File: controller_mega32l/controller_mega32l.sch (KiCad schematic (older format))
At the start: 82 parts, among them IC1 ATMEGA32-A, IC2 MAX481CPA, J1 RJ45, K1 CONN_PWR_OUT, P1 CONN_PWR_IN, P2 CONN_PWM_OUT, P3 CONN_3X2, P4 CONN_JTAG, P5 CONN_ADC, P6 CONN_GPIO, Q1 NPN

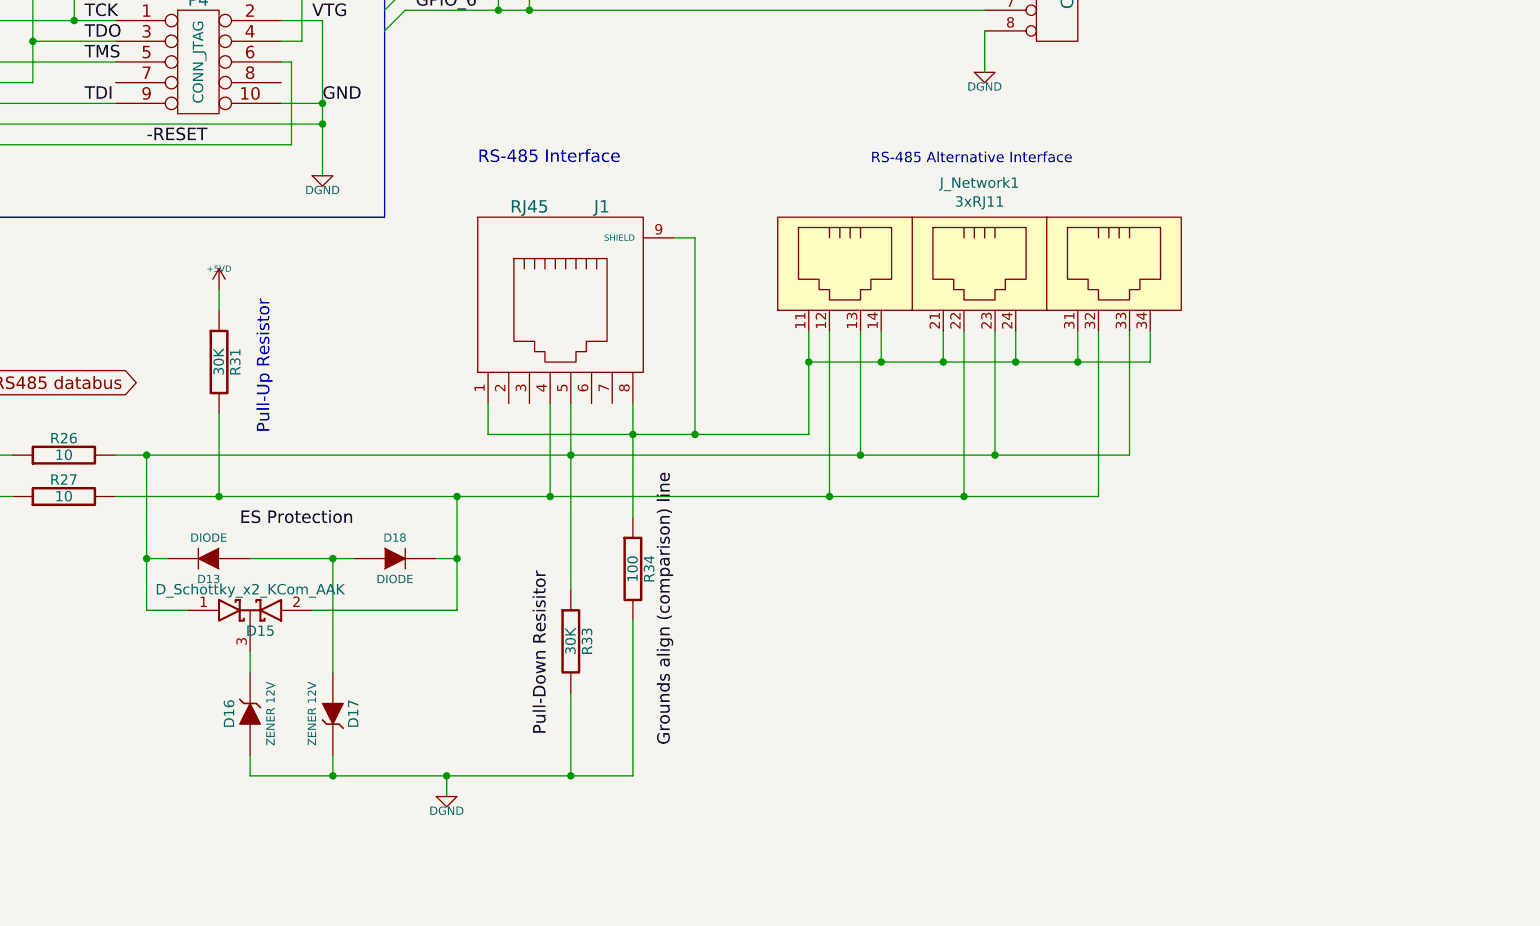
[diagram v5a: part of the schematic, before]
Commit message: Output RJ-45 Interfaces added
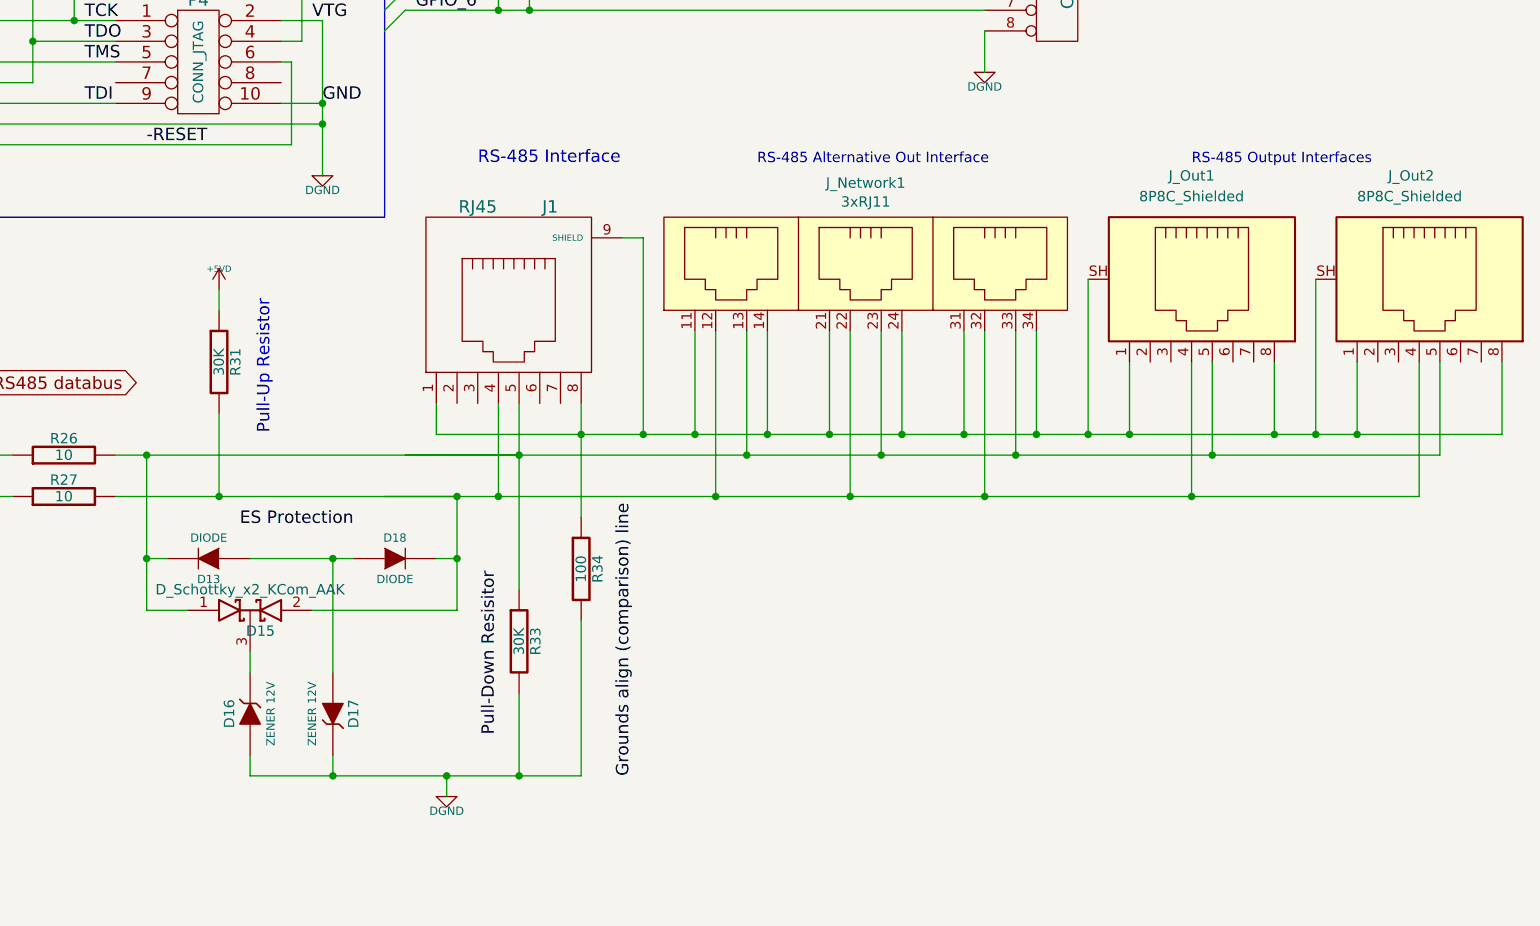
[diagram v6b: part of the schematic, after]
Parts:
- added J_Out1, J_Out2: 8P8C_Shielded, Connector_RJ:RJ45_Amphenol_54602-x08_Horizontal, symbol Connector:8P8C_Shielded
- J1: footprint RJ45_8 -> Connector_RJ:RJ45_Amphenol_54602-x08_Horizontal
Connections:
- net at J1.1, J1.8, J1.9 (SHIELD)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: now also J_Out1.1, J_Out1.8, J_Out1.SH, J_Out2.1, J_Out2.8, J_Out2.SH
- net at D15.2 (A), D18.2 (K), J1.4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: now also J_Out1.4, J_Out2.4
- net at D13.2 (K), D15.1 (A), J1.5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: now also J_Out1.5, J_Out2.5
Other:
- note added: "RS-485 Alternative Out Interface"
- note added: "RS-485 Output Interfaces"
- note removed: "RS-485 Alternative Interface"
- moved on the sheet: J1, J_Network1, R33, R34
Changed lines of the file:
@@
 Text Label 11300 11800 0    60   ~ 0
 ES Protection
-Text Label 13400 12850 1    60   ~ 0
+Text Label 13200 13000 1    60   ~ 0
 Grounds align (comparison) line
-Text Label 12800 12800 1    60   ~ 0
+Text Label 12550 12800 1    60   ~ 0
 Pull-Down Resisitor
 $Comp
@@
 L controller_mega32l-rescue:R-RESCUE-controller_mega32l R33
 U 1 1 4DBDE50D
-P 12900 12350
-F 0 "R33" V 12980 12350 50  0000 C CNN
-F 1 "30K" V 12900 12350 50  0000 C CNN
-F 2 "SM0603" H 12900 12350 60  0001 C CNN
-F 3 "" H 12900 12350 60  0001 C CNN
-	1    12900 12350
+P 12650 12350
+F 0 "R33" V 12730 12350 50  0000 C CNN
+F 1 "30K" V 12650 12350 50  0000 C CNN
+F 2 "SM0603" H 12650 12350 60  0001 C CNN
+F 3 "" H 12650 12350 60  0001 C CNN
+	1    12650 12350
 	1    0    0    -1
 $EndComp
@@
 L controller_mega32l-rescue:R-RESCUE-controller_mega32l R34
 U 1 1 4DBDE4EF
-P 13200 12000
-F 0 "R34" V 13280 12000 50  0000 C CNN
-F 1 "100" V 13200 12000 50  0000 C CNN
-F 2 "C1" H 13200 12000 60  0001 C CNN
-F 3 "" H 13200 12000 60  0001 C CNN
-	1    13200 12000
+P 12950 12000
+F 0 "R34" V 13030 12000 50  0000 C CNN
+F 1 "100" V 12950 12000 50  0000 C CNN
+F 2 "C1" H 12950 12000 60  0001 C CNN
+F 3 "" H 12950 12000 60  0001 C CNN
+	1    12950 12000
 	1    0    0    -1
 $EndComp
@@
 L controller_mega32l-rescue:RJ45 J1
 U 1 1 4DB1B186
-P 12850 10750
-F 0 "J1" H 13050 11250 60  0000 C CNN
-F 1 "RJ45" H 12700 11250 60  0000 C CNN
-F 2 "RJ45_8" H 12850 10750 60  0001 C CNN
-F 3 "" H 12850 10750 60  0001 C CNN
-	1    12850 10750
+P 12600 10750
+F 0 "J1" H 12800 11250 60  0000 C CNN
+F 1 "RJ45" H 12450 11250 60  0000 C CNN
+F 2 "Connector_RJ:RJ45_Amphenol_54602-x08_Horizontal" H 12600 10750 60  0001 C CNN
+F 3 "" H 12600 10750 60  0001 C CNN
+	1    12600 10750
 	1    0    0    -1
 $EndComp
@@
 	3900 5550 3900 5500
 Wire Wire Line
-	13500 10400 13400 10400
+	13250 10400 13150 10400
 Connection ~ 4400 6750
 Wire Wire Line
@@
 Wire Wire Line
 	11200 11250 11200 11650
-Connection ~ 12900 13000
-Wire Wire Line
-	12900 13000 12900 12600
+Wire Wire Line
+	12650 13000 12650 12600
 Connection ~ 12300 13000
 Wire Wire Line
 	12300 13000 12300 13100
 Wire Wire Line
-	13200 11200 13200 11350
+	12950 11200 12950 11350
 Connection ~ 12350 11650
 Wire Wire Line
 	10700 11650 11200 11650
 Wire Wire Line
-	12800 11650 12800 11200
+	12550 11650 12550 11200
 Connection ~ 10850 11950
 Wire Wire Line
@@
 Connection ~ 10850 11450
 Wire Wire Line
-	12900 11200 12900 11450
-Connection ~ 12900 11450
-Wire Wire Line
-	13200 13000 13200 12250
+	12650 11200 12650 11450
+Wire Wire Line
+	12950 13000 12950 12250
 Wire Wire Line
 	11350 13000 11750 13000
@@
 	9100 4900 9250 4900
 Wire Wire Line
-	11200 11650 12350 11650
-Wire Wire Line
-	12900 13000 13200 13000
-Wire Wire Line
-	12300 13000 12900 13000
-Wire Wire Line
-	12350 11650 12800 11650
+	12300 13000 12650 13000
 Wire Wire Line
 	10850 11950 10850 12200
@@
 	11750 11950 11850 11950
 Wire Wire Line
-	10850 11450 12900 11450
-Wire Wire Line
-	12900 11450 12900 12100
+	12650 11450 12650 12100
 Wire Wire Line
 	11750 13000 12300 13000
@@
 Wire Wire Line
 	12150 7400 12700 7400
-Text Notes 14350 10050 0    50   ~ 0
-RS-485 Alternative Interface
-Wire Wire Line
-	12500 11200 12500 11350
-Wire Wire Line
-	12500 11350 13200 11350
-Connection ~ 13200 11350
-Wire Wire Line
-	13200 11350 13200 11750
-Wire Wire Line
-	15450 11650 15450 10850
-Wire Wire Line
-	14800 11650 15450 11650
-Wire Wire Line
-	14800 11650 14800 10850
-Connection ~ 14800 11650
-Wire Wire Line
-	14150 11650 14800 11650
-Wire Wire Line
-	14950 11450 15600 11450
-Wire Wire Line
-	14950 11450 14950 10850
-Connection ~ 14950 11450
-Wire Wire Line
-	14300 11450 14950 11450
-Wire Wire Line
-	15600 11450 15600 10850
-Wire Wire Line
-	15700 11000 15700 10850
-Wire Wire Line
-	15350 11000 15700 11000
-Wire Wire Line
-	15350 11000 15350 10850
-Connection ~ 15350 11000
-Wire Wire Line
-	15050 11000 15350 11000
-Wire Wire Line
-	15050 11000 15050 10850
-Connection ~ 15050 11000
-Wire Wire Line
-	14700 11000 15050 11000
-Wire Wire Line
-	14700 11000 14700 10850
-Connection ~ 14700 11000
-Wire Wire Line
-	14400 11000 14700 11000
-Wire Wire Line
-	14400 11000 14400 10850
-Connection ~ 14400 11000
-Wire Wire Line
-	14050 11000 14400 11000
-Wire Wire Line
-	14050 10850 14050 11000
-Wire Wire Line
-	14300 11450 14300 10850
-Connection ~ 14300 11450
-Wire Wire Line
-	12900 11450 14300 11450
-Wire Wire Line
-	14150 11650 14150 10850
-Connection ~ 14150 11650
-Connection ~ 12800 11650
-Wire Wire Line
-	12800 11650 14150 11650
+Wire Wire Line
+	12250 11200 12250 11350
+Connection ~ 12950 11350
+Wire Wire Line
+	12950 11350 12950 11750
+Wire Wire Line
+	13250 10400 13250 11350
+Wire Wire Line
+	13250 11350 12950 11350
+$Comp
+L Connector:8P8C_Shielded J_Out1
+U 1 1 60063DF9
+P 15900 10600
+F 0 "J_Out1" V 15400 10600 50  0000 C CNN
+F 1 "8P8C_Shielded" V 15500 10600 50  0000 C CNN
+F 2 "Connector_RJ:RJ45_Amphenol_54602-x08_Horizontal" V 15900 10625 50  0001 C CNN
+F 3 "~" V 15900 10625 50  0001 C CNN
+	1    15900 10600
+	0    1    1    0
+$EndComp
+$Comp
+L Connector:8P8C_Shielded J_Out2
+U 1 1 60066A48
+P 17000 10600
+F 0 "J_Out2" V 16500 10450 50  0000 L CNN
+F 1 "8P8C_Shielded" V 16600 10300 50  0000 L CNN
+F 2 "Connector_RJ:RJ45_Amphenol_54602-x08_Horizontal" V 17000 10625 50  0001 C CNN
+F 3 "~" V 17000 10625 50  0001 C CNN
+	1    17000 10600
+	0    1    1    0
+$EndComp
+Wire Wire Line
+	12250 11350 12950 11350
+Wire Wire Line
+	12350 11650 12550 11650
 $Comp
 L CustomLibrary:3xRJ11 J_Network1
 U 1 1 5CF90E57
-P 13850 10150
-F 0 "J_Network1" H 14875 10165 50  0000 C CNN
-F 1 "3xRJ11" H 14875 10074 50  0000 C CNN
-F 2 "" H 14250 10050 50  0001 C CNN
-F 3 "" H 14250 10050 50  0001 C CNN
-	1    13850 10150
-	1    0    0    -1
-$EndComp
-Wire Wire Line
-	13500 10400 13500 11350
-Wire Wire Line
-	13500 11350 13200 11350
-Wire Wire Line
-	13500 11350 14050 11350
-Wire Wire Line
-	14050 11350 14050 11000
+P 13300 10150
+F 0 "J_Network1" H 14325 10165 50  0000 C CNN
+F 1 "3xRJ11" H 14325 10074 50  0000 C CNN
+F 2 "" H 13700 10050 50  0001 C CNN
+F 3 "" H 13700 10050 50  0001 C CNN
+	1    13300 10150
+	1    0    0    -1
+$EndComp
+Connection ~ 13600 11650
+Wire Wire Line
+	13600 11650 13600 10850
+Connection ~ 13750 11450
+Wire Wire Line
+	13750 11450 13750 10850
+Wire Wire Line
+	15050 11450 15050 10850
+Wire Wire Line
+	13750 11450 14400 11450
+Connection ~ 14400 11450
+Wire Wire Line
+	14400 11450 14400 10850
+Wire Wire Line
+	14400 11450 15050 11450
+Wire Wire Line
+	13600 11650 14250 11650
+Connection ~ 14250 11650
+Wire Wire Line
+	14250 11650 14250 10850
+Wire Wire Line
+	14250 11650 14900 11650
+Wire Wire Line
+	14900 11650 14900 10850
+Text Notes 13800 10050 0    50   ~ 0
+RS-485 Alternative Out Interface
+Connection ~ 12650 11450
+Connection ~ 12650 13000
+Wire Wire Line
+	12650 13000 12950 13000
+Connection ~ 12550 11650
+Connection ~ 13250 11350
+Wire Wire Line
+	13250 11350 13500 11350
+Wire Wire Line
+	12650 11450 13750 11450
+Wire Wire Line
+	12550 11650 13600 11650
+Wire Wire Line
+	12000 11650 12350 11650
+Wire Wire Line
+	12100 11450 12650 11450
+Wire Wire Line
+	11200 11650 12350 11650
+Wire Wire Line
+	10850 11450 12650 11450
+Wire Wire Line
+	13500 11350 13850 11350
+Wire Wire Line
+	17400 11350 17400 11000
+Connection ~ 13500 11350
+Wire Wire Line
+	16700 11000 16700 11350
+Connection ~ 16700 11350
+Wire Wire Line
+	16700 11350 17400 11350
+Wire Wire Line
+	16300 11000 16300 11350
+Connection ~ 16300 11350
+Wire Wire Line
+	16300 11350 16500 11350
+Wire Wire Line
+	15600 11000 15600 11350
+Connection ~ 15600 11350
+Wire Wire Line
+	15600 11350 16300 11350
+Wire Wire Line
+	15400 10600 15400 11350
+Connection ~ 15400 11350
+Wire Wire Line
+	15400 11350 15600 11350
+Wire Wire Line
+	16500 10600 16500 11350
+Connection ~ 16500 11350
+Wire Wire Line
+	16500 11350 16700 11350
+Connection ~ 15150 11350
+Wire Wire Line
+	15150 11350 15400 11350
+Wire Wire Line
+	13500 10850 13500 11350
+Wire Wire Line
+	15150 10850 15150 11350
+Wire Wire Line
+	14800 10850 14800 11350
+Connection ~ 14800 11350
+Wire Wire Line
+	14800 11350 15150 11350
+Wire Wire Line
+	14500 10850 14500 11350
+Connection ~ 14500 11350
+Wire Wire Line
+	14500 11350 14800 11350
+Wire Wire Line
+	14150 10850 14150 11350
+Connection ~ 14150 11350
+Wire Wire Line
+	14150 11350 14500 11350
+Wire Wire Line
+	13850 10850 13850 11350
+Connection ~ 13850 11350
+Wire Wire Line
+	13850 11350 14150 11350
+Wire Wire Line
+	15050 11450 16000 11450
+Wire Wire Line
+	17100 11450 17100 11000
+Connection ~ 15050 11450
+Wire Wire Line
+	14900 11650 15900 11650
+Wire Wire Line
+	17000 11650 17000 11000
+Connection ~ 14900 11650
+Wire Wire Line
+	16000 11000 16000 11450
+Connection ~ 16000 11450
+Wire Wire Line
+	16000 11450 17100 11450
+Wire Wire Line
+	15900 11000 15900 11650
+Connection ~ 15900 11650
+Wire Wire Line
+	15900 11650 17000 11650
+Text Notes 15900 10050 0    50   ~ 0
+RS-485 Output Interfaces
 Wire Wire Line
 	7350 8350 8600 8350
@@
 Wire Bus Line
 	8500 8350 8500 10300
-Connection ~ 13500 11350
-Connection ~ 14050 11000
 $EndSCHEMATC
